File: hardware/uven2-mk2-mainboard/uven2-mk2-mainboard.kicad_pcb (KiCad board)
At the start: 2 copper layers, 121 x 93 mm, 87 parts, among them J1 LED, J10 LED, J11 LED, J12 LED, J13 LED, J14 LED, J15 LED, J16 LED, J2 LED, J3 LED, J4 LED, J5 LED, J6 LED, J7 LED, J8 LED, J9 LED, Q1 QM6006D, Q10 QM6006D, Q11 QM6006D, Q12 QM6006D, Q13 QM6006D, Q14 QM6006D, Q15 QM6006D, Q16 QM6006D, Q2 QM6006D, Q3 QM6006D, Q4 QM6006D, Q5 QM6006D, Q6 QM6006D, Q7 QM6006D, Q8 QM6006D, Q9 QM6006D, U1 DEV-16771, U2 MCP48FEB28T-20E/ST, U3 MCP48FEB28T-20E/ST

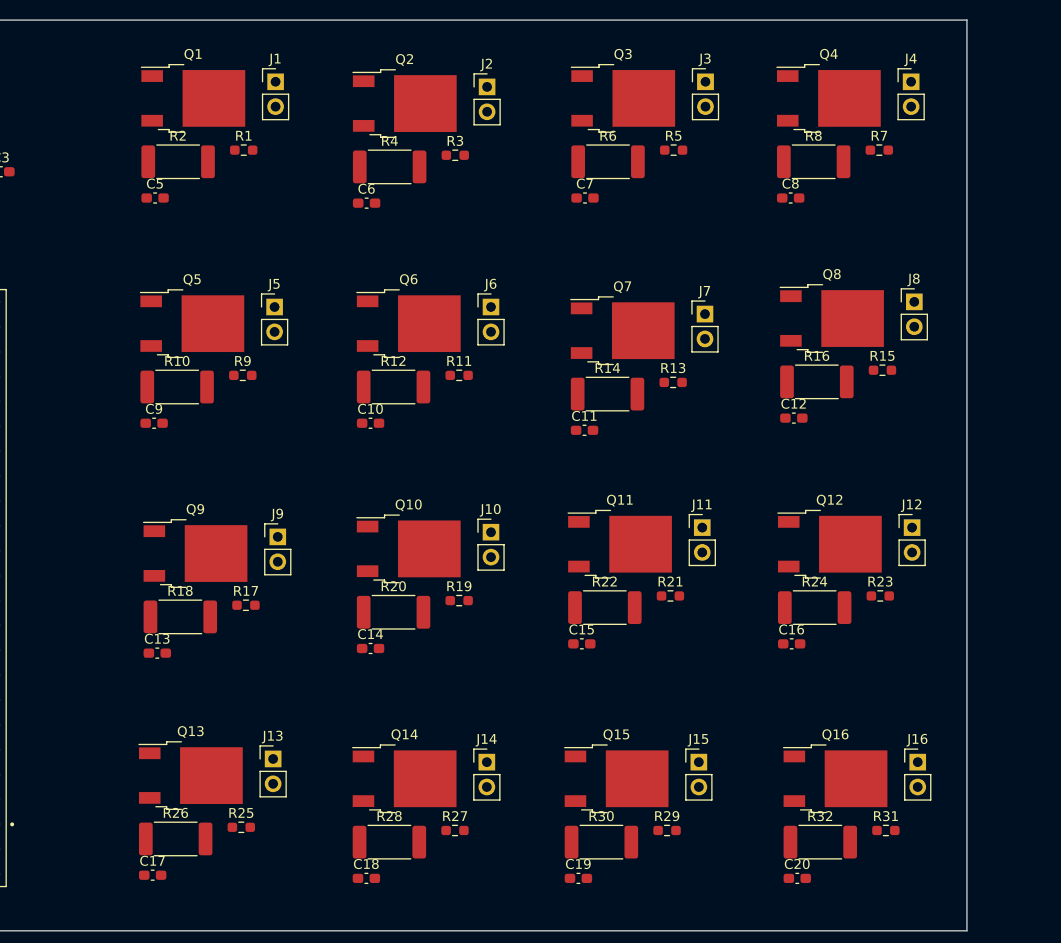
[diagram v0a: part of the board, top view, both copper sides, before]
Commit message: with current limiting switch
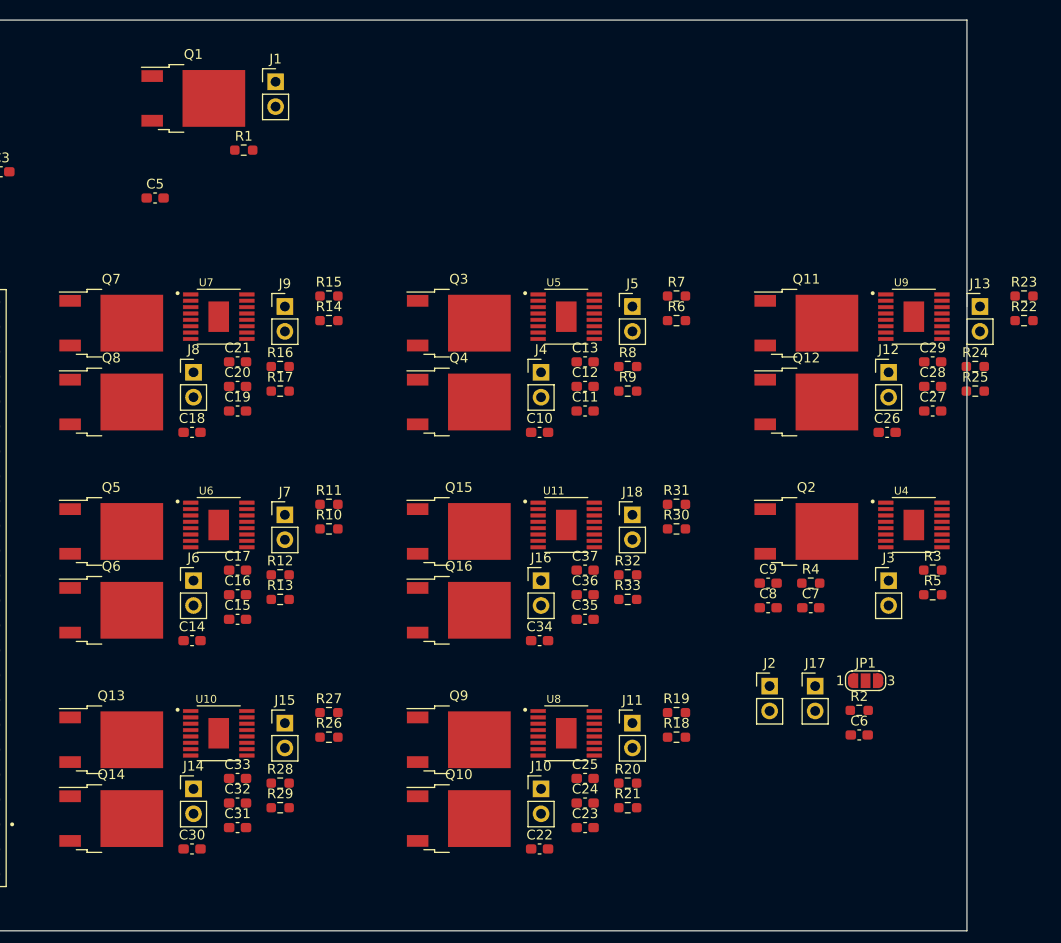
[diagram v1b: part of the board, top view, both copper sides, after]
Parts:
- added C21: 4.7u, Capacitor_SMD:C_0603_1608Metric_Pad1.08x0.95mm_HandSolder, F.Cu at (131.5, 72.9)
- added C22: 100n, Capacitor_SMD:C_0603_1608Metric_Pad1.08x0.95mm_HandSolder, F.Cu at (162.4, 122.6)
- added C23: 100n, Capacitor_SMD:C_0603_1608Metric_Pad1.08x0.95mm_HandSolder, F.Cu at (167.0, 120.5)
- added C24: 220n, Capacitor_SMD:C_0603_1608Metric_Pad1.08x0.95mm_HandSolder, F.Cu at (167.0, 118.0)
- added C25: 4.7u, Capacitor_SMD:C_0603_1608Metric_Pad1.08x0.95mm_HandSolder, F.Cu at (167.0, 115.4)
- added C26: 100n, Capacitor_SMD:C_0603_1608Metric_Pad1.08x0.95mm_HandSolder, F.Cu at (197.8, 80.1)
- added C27: 100n, Capacitor_SMD:C_0603_1608Metric_Pad1.08x0.95mm_HandSolder, F.Cu at (202.5, 77.9)
- added C28: 220n, Capacitor_SMD:C_0603_1608Metric_Pad1.08x0.95mm_HandSolder, F.Cu at (202.5, 75.4)
- added C29: 4.7u, Capacitor_SMD:C_0603_1608Metric_Pad1.08x0.95mm_HandSolder, F.Cu at (202.5, 72.9)
- added C30: 100n, Capacitor_SMD:C_0603_1608Metric_Pad1.08x0.95mm_HandSolder, F.Cu at (126.9, 122.6)
- added C31: 100n, Capacitor_SMD:C_0603_1608Metric_Pad1.08x0.95mm_HandSolder, F.Cu at (131.5, 120.5)
- added C32: 220n, Capacitor_SMD:C_0603_1608Metric_Pad1.08x0.95mm_HandSolder, F.Cu at (131.5, 118.0)
- added C33: 4.7u, Capacitor_SMD:C_0603_1608Metric_Pad1.08x0.95mm_HandSolder, F.Cu at (131.5, 115.4)
- added C34: 100n, Capacitor_SMD:C_0603_1608Metric_Pad1.08x0.95mm_HandSolder, F.Cu at (162.4, 101.4)
- added C35: 100n, Capacitor_SMD:C_0603_1608Metric_Pad1.08x0.95mm_HandSolder, F.Cu at (167.0, 99.2)
- added C36: 220n, Capacitor_SMD:C_0603_1608Metric_Pad1.08x0.95mm_HandSolder, F.Cu at (167.0, 96.7)
- added C37: 4.7u, Capacitor_SMD:C_0603_1608Metric_Pad1.08x0.95mm_HandSolder, F.Cu at (167.0, 94.2)
- added J17: PowerON/OFF, Connector_PinHeader_2.54mm:PinHeader_1x02_P2.54mm_Vertical, F.Cu at (190.5, 106.0)
- added J18: LED, Connector_PinHeader_2.54mm:PinHeader_1x02_P2.54mm_Vertical, F.Cu at (171.8, 88.5)
- added JP1: Vref_select, Jumper:SolderJumper-3_P1.3mm_Open_RoundedPad1.0x1.5mm_NumberLabels, F.Cu at (195.7, 105.5)
- added R33: 10k, Resistor_SMD:R_0603_1608Metric_Pad0.98x0.95mm_HandSolder, F.Cu at (171.4, 97.2)
- added U10: TPS2HB50BQPWPRQ1, custom_lib:SOP65P640X120-17N, F.Cu at (129.6, 110.8)
- added U11: TPS2HB50BQPWPRQ1, custom_lib:SOP65P640X120-17N, F.Cu at (165.1, 89.6)
- added U4: TPS2HB50BQPWPRQ1, custom_lib:SOP65P640X120-17N, F.Cu at (200.6, 89.6)
- added U5: TPS2HB50BQPWPRQ1, custom_lib:SOP65P640X120-17N, F.Cu at (165.1, 68.3)
- added U6: TPS2HB50BQPWPRQ1, custom_lib:SOP65P640X120-17N, F.Cu at (129.6, 89.6)
- added U7: TPS2HB50BQPWPRQ1, custom_lib:SOP65P640X120-17N, F.Cu at (129.6, 68.3)
- added U8: TPS2HB50BQPWPRQ1, custom_lib:SOP65P640X120-17N, F.Cu at (165.1, 110.8)
- added U9: TPS2HB50BQPWPRQ1, custom_lib:SOP65P640X120-17N, F.Cu at (200.6, 68.3)
- C12, C16, C20, C8: value 100n -> 220n
- C13, C17, C9: value 100n -> 4.7u
- C6: value 100n -> 10n
- J2: value LED -> LED_ENABLE
- R10, R14, R18, R2, R22, R26, R30, R6: value 220mOhm -> 1k; footprint Resistor_SMD:R_2512_6332Metric_Pad1.40x3.35mm_HandSolder -> Resistor_SMD:R_0603_1608Metric_Pad0.98x0.95mm_HandSolder
- R12, R16, R20, R24, R28, R32, R4, R8: value 220mOhm -> 10k; footprint Resistor_SMD:R_2512_6332Metric_Pad1.40x3.35mm_HandSolder -> Resistor_SMD:R_0603_1608Metric_Pad0.98x0.95mm_HandSolder
- R13, R17, R21, R25, R29, R5, R9: value 1k -> 10k
- moved R2 89.3 mm to (195.0, 108.5)
- moved R25 87.2 mm to (206.8, 75.9)
- moved J13 85.7 mm to (207.3, 67.2)
- moved C20 76.1 mm to (131.5, 75.4)
- moved Q8 74.1 mm to (118.6, 77.0)
- moved C6 74.0 mm to (195.0, 111.0)
- moved J8 74.0 mm to (127.0, 74.0)
- moved J2 67.6 mm to (185.8, 106.0)
- moved C9 64.8 mm to (185.7, 95.5)
- moved R3 64.6 mm to (202.5, 94.2)
- moved R4 60.5 mm to (190.1, 95.5)
- moved Q2 59.9 mm to (189.6, 90.2)
- moved C19 59.1 mm to (131.5, 77.9)
- moved R15 57.0 mm to (140.8, 66.2)
- moved C16 56.8 mm to (131.5, 96.7)
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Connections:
- C10 pad 2: /GATE_LED5 -> /GATE_LED2
- C11 pad 2: /GATE_LED6 -> /GATE_LED3
- C12 pad 2: /GATE_LED7 -> +24V
- C13 pad 2: /GATE_LED8 -> +24V
- C14 pad 2: /GATE_LED9 -> /GATE_LED4
- C15 pad 2: /GATE_LED10 -> /GATE_LED5
- C16 pad 2: /GATE_LED11 -> +24V
- C17 pad 2: /GATE_LED12 -> +24V
- C18 pad 2: /GATE_LED13 -> /GATE_LED6
- C19 pad 2: /GATE_LED14 -> /GATE_LED7
- C20 pad 2: /GATE_LED15 -> +24V
- C6 pad 1: GND -> /LED_SENS
- C6 pad 2: /GATE_LED1 -> GND
- C7 pad 2: /GATE_LED2 -> /GATE_LED1
- C8 pad 2: /GATE_LED3 -> +24V
- C9 pad 2: /GATE_LED4 -> +24V
- J1 pad 1: +24V -> unconnected-(J1-Pad1)
- J10 pad 1: +24V -> unconnected-(J10-Pad1)
- J11 pad 1: +24V -> unconnected-(J11-Pad1)
- J12 pad 1: +24V -> unconnected-(J12-Pad1)
- J13 pad 1: +24V -> unconnected-(J13-Pad1)
- J14 pad 1: +24V -> unconnected-(J14-Pad1)
- J15 pad 1: +24V -> unconnected-(J15-Pad1)
- J16 pad 1: +24V -> unconnected-(J16-Pad1)
- J2 pad 1: +24V -> GND
- J2 pad 2: Net-(J2-Pad2) -> /LED_ENABLE
- J3 pad 1: +24V -> unconnected-(J3-Pad1)
- J4 pad 1: +24V -> unconnected-(J4-Pad1)
- J5 pad 1: +24V -> unconnected-(J5-Pad1)
- J6 pad 1: +24V -> unconnected-(J6-Pad1)
- J7 pad 1: +24V -> unconnected-(J7-Pad1)
- J8 pad 1: +24V -> unconnected-(J8-Pad1)
- J9 pad 1: +24V -> unconnected-(J9-Pad1)
- Q1 pad 3: /SHUNT_LED0 -> GND
- Q10 pad 2: Net-(J10-Pad2) -> Net-(J11-Pad2)
- Q10 pad 3: /SHUNT_LED9 -> GND
- Q11 pad 2: Net-(J11-Pad2) -> Net-(J12-Pad2)
- Q11 pad 3: /SHUNT_LED10 -> GND
- Q12 pad 2: Net-(J12-Pad2) -> Net-(J13-Pad2)
- Q12 pad 3: /SHUNT_LED11 -> GND
- Q13 pad 2: Net-(J13-Pad2) -> Net-(J14-Pad2)
- Q13 pad 3: /SHUNT_LED12 -> GND
- Q14 pad 2: Net-(J14-Pad2) -> Net-(J15-Pad2)
- Q14 pad 3: /SHUNT_LED13 -> GND
- Q15 pad 2: Net-(J15-Pad2) -> Net-(J16-Pad2)
- Q15 pad 3: /SHUNT_LED14 -> GND
- Q16 pad 2: Net-(J16-Pad2) -> Net-(J18-Pad2)
- Q16 pad 3: /SHUNT_LED15 -> GND
- Q2 pad 2: Net-(J2-Pad2) -> Net-(J3-Pad2)
- Q2 pad 3: /SHUNT_LED1 -> GND
- Q3 pad 2: Net-(J3-Pad2) -> Net-(J4-Pad2)
- Q3 pad 3: /SHUNT_LED2 -> GND
- Q4 pad 2: Net-(J4-Pad2) -> Net-(J5-Pad2)
- Q4 pad 3: /SHUNT_LED3 -> GND
- Q5 pad 2: Net-(J5-Pad2) -> Net-(J6-Pad2)
- Q5 pad 3: /SHUNT_LED4 -> GND
- Q6 pad 2: Net-(J6-Pad2) -> Net-(J7-Pad2)
- Q6 pad 3: /SHUNT_LED5 -> GND
- Q7 pad 2: Net-(J7-Pad2) -> Net-(J8-Pad2)
- Q7 pad 3: /SHUNT_LED6 -> GND
- Q8 pad 2: Net-(J8-Pad2) -> Net-(J9-Pad2)
- Q8 pad 3: /SHUNT_LED7 -> GND
- Q9 pad 2: Net-(J9-Pad2) -> Net-(J10-Pad2)
- Q9 pad 3: /SHUNT_LED8 -> GND
- R10 pad 1: /SHUNT_LED4 -> GND
- R10 pad 2: GND -> /GATE_LED4
- R12 pad 1: /SHUNT_LED5 -> +24V
- R12 pad 2: GND -> Net-(R12-Pad2)
- R13 pad 1: GND -> +24V
- R13 pad 2: /GATE_LED6 -> Net-(R13-Pad2)
- R14 pad 1: /SHUNT_LED6 -> GND
- R14 pad 2: GND -> /GATE_LED6
- R16 pad 1: /SHUNT_LED7 -> +24V
- R16 pad 2: GND -> Net-(R16-Pad2)
- R17 pad 1: GND -> +24V
- R17 pad 2: /GATE_LED8 -> Net-(R17-Pad2)
- R18 pad 1: /SHUNT_LED8 -> GND
- R18 pad 2: GND -> /GATE_LED8
- R2 pad 1: /SHUNT_LED0 -> /LED_SENS
- R20 pad 1: /SHUNT_LED9 -> +24V
- R20 pad 2: GND -> Net-(R20-Pad2)
- R21 pad 1: GND -> +24V
- R21 pad 2: /GATE_LED10 -> Net-(R21-Pad2)
- R22 pad 1: /SHUNT_LED10 -> GND
- R22 pad 2: GND -> /GATE_LED10
- R24 pad 1: /SHUNT_LED11 -> +24V
- R24 pad 2: GND -> Net-(R24-Pad2)
- R25 pad 1: GND -> +24V
- R25 pad 2: /GATE_LED12 -> Net-(R25-Pad2)
- R26 pad 1: /SHUNT_LED12 -> GND
- R26 pad 2: GND -> /GATE_LED12
- R28 pad 1: /SHUNT_LED13 -> +24V
- R28 pad 2: GND -> Net-(R28-Pad2)
- R29 pad 1: GND -> +24V
- R29 pad 2: /GATE_LED14 -> Net-(R29-Pad2)
- R30 pad 1: /SHUNT_LED14 -> GND
- R30 pad 2: GND -> /GATE_LED14
- R32 pad 1: /SHUNT_LED15 -> +24V
- R32 pad 2: GND -> Net-(R32-Pad2)
- R4 pad 1: /SHUNT_LED1 -> +24V
- R4 pad 2: GND -> Net-(R4-Pad2)
- R5 pad 1: GND -> +24V
- R5 pad 2: /GATE_LED2 -> Net-(R5-Pad2)
- R6 pad 1: /SHUNT_LED2 -> GND
- R6 pad 2: GND -> /GATE_LED2
- R8 pad 1: /SHUNT_LED3 -> +24V
- R8 pad 2: GND -> Net-(R8-Pad2)
- R9 pad 1: GND -> +24V
- R9 pad 2: /GATE_LED4 -> Net-(R9-Pad2)
- U1 pad 14: /SHUNT_LED0 -> /LED_SENS
- U1 pad 15: /SHUNT_LED1 -> /LED_DIAG_ENABLE_A
- U1 pad 16: /SHUNT_LED2 -> /LED_DIAG_ENABLE_B
- U1 pad 17: /SHUNT_LED3 -> /LED_DIAG_ENABLE_C
- U1 pad 18: /SHUNT_LED4 -> /LED_DIAG_ENABLE_D
- U1 pad 19: /SHUNT_LED5 -> /LED_DIAG_ENABLE_E
- U1 pad 20: /SHUNT_LED6 -> /LED_DIAG_ENABLE_F
- U1 pad 21: /SHUNT_LED7 -> /LED_DIAG_ENABLE_G
- U1 pad 22: /SHUNT_LED8 -> /LED_DIAG_ENABLE_H
- U1 pad 23: /SHUNT_LED9 -> /LED_ENABLE
- U1 pad 24: /SHUNT_LED10 -> /LED_LATCH
- U1 pad 25: /SHUNT_LED11 -> /LED0_SEL
- U1 pad 26: /SHUNT_LED12 -> /LED1_SEL
- U1 pad 27: /SHUNT_LED13 -> /LATCH0
- U1 pad 38: /SHUNT_LED14 -> /LATCH1
- U1 pad 39: /SHUNT_LED15 -> unconnected-(U1-Pad39)
- U1 pad 5V: unconnected-(U1-Pad5V) -> +5V
- U1 pad GND1: Net-(U1-PadGND1) -> GND
- U1 pad GND2: Net-(U1-PadGND1) -> GND
- U1 pad GND3: Net-(U1-PadGND1) -> GND
- U1 pad GND4: Net-(U1-PadGND1) -> GND
- U1 pad GND5: Net-(U1-PadGND1) -> GND
- U1 pad ON/OFF: unconnected-(U1-PadON/OFF) -> /PowerON/OFF
- U1 pad USB_GND1: Net-(U1-PadUSB_GND1) -> GND
- U1 pad USB_GND2: Net-(U1-PadUSB_GND1) -> GND
- U2 pad 16: +3.3V -> Net-(U2-Pad16)
- U2 pad 4: +3.3V -> Net-(U2-Pad16)

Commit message: with wago connector
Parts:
- removed J10, J11, J12, J13, J14, J15, J16, J18, J3, J4, J5, J6, J7, J8, J9: LED, Connector_PinHeader_2.54mm:PinHeader_1x02_P2.54mm_Vertical
- J1: value LED -> 713-1436_037-000; footprint Connector_PinHeader_2.54mm:PinHeader_1x02_P2.54mm_Vertical -> custom_lib:CONN_713-1436&slash_037-000_WAG
- moved J1 63.7 mm to (199.0, 48.0), turned to 180 degrees
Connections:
- J1 pad 1: unconnected-(J1-Pad1) -> /LED0-
- J1 pad 2: Net-(J1-Pad2) -> /LED0+
- Q1 pad 2: Net-(J1-Pad2) -> /LED0-
- Q10 pad 2: Net-(J11-Pad2) -> /LED9-
- Q11 pad 2: Net-(J12-Pad2) -> /LED10-
- Q12 pad 2: Net-(J13-Pad2) -> /LED11-
- Q13 pad 2: Net-(J14-Pad2) -> /LED12-
- Q14 pad 2: Net-(J15-Pad2) -> /LED13-
- Q15 pad 2: Net-(J16-Pad2) -> /LED14-
- Q16 pad 2: Net-(J18-Pad2) -> /LED15-
- Q2 pad 2: Net-(J3-Pad2) -> /LED1-
- Q3 pad 2: Net-(J4-Pad2) -> /LED2-
- Q4 pad 2: Net-(J5-Pad2) -> /LED3-
- Q5 pad 2: Net-(J6-Pad2) -> /LED4-
- Q6 pad 2: Net-(J7-Pad2) -> /LED5-
- Q7 pad 2: Net-(J8-Pad2) -> /LED6-
- Q8 pad 2: Net-(J9-Pad2) -> /LED7-
- Q9 pad 2: Net-(J10-Pad2) -> /LED8-
- U1 pad 15: /LED_DIAG_ENABLE_A -> /TEMP_LED0
- U1 pad 16: /LED_DIAG_ENABLE_B -> /TEMP_LED1
- U1 pad 17: /LED_DIAG_ENABLE_C -> /TEMP_LED2
- U1 pad 18: /LED_DIAG_ENABLE_D -> /TEMP_LED3
- U1 pad 19: /LED_DIAG_ENABLE_E -> /TEMP_LED4
- U1 pad 2: unconnected-(U1-Pad2) -> /LED_ENABLE
- U1 pad 20: /LED_DIAG_ENABLE_F -> /TEMP_LED5
- U1 pad 21: /LED_DIAG_ENABLE_G -> /TEMP_LED6
- U1 pad 22: /LED_DIAG_ENABLE_H -> /TEMP_LED7
- U1 pad 23: /LED_ENABLE -> /TEMP_LED8
- U1 pad 24: /LED_LATCH -> /TEMP_LED9
- U1 pad 25: /LED0_SEL -> /TEMP_LED10
- U1 pad 26: /LED1_SEL -> /TEMP_LED11
- U1 pad 27: /LATCH0 -> /TEMP_LED12
- U1 pad 28: unconnected-(U1-Pad28) -> /LED_DIAG_ENABLE_C
- U1 pad 29: unconnected-(U1-Pad29) -> /LED_DIAG_ENABLE_D
- U1 pad 3: unconnected-(U1-Pad3) -> /LED_LATCH
- U1 pad 30: unconnected-(U1-Pad30) -> /LED_DIAG_ENABLE_E
- U1 pad 31: unconnected-(U1-Pad31) -> /LED_DIAG_ENABLE_F
- U1 pad 33: unconnected-(U1-Pad33) -> /LED_DIAG_ENABLE_G
- U1 pad 34: unconnected-(U1-Pad34) -> /LED_DIAG_ENABLE_H
- U1 pad 38: /LATCH1 -> /TEMP_LED13
- U1 pad 39: unconnected-(U1-Pad39) -> /TEMP_LED14
- U1 pad 4: unconnected-(U1-Pad4) -> /LED0_SEL
- U1 pad 40: unconnected-(U1-Pad40) -> /TEMP_LED15
- U1 pad 5: unconnected-(U1-Pad5) -> /LED1_SEL
- U1 pad 6: unconnected-(U1-Pad6) -> /LATCH0
- U1 pad 7: unconnected-(U1-Pad7) -> /LATCH1
- U1 pad 8: unconnected-(U1-Pad8) -> /LED_DIAG_ENABLE_A
- U1 pad 9: unconnected-(U1-Pad9) -> /LED_DIAG_ENABLE_B
- U10 pad 10: /LED Driver6/LED1 -> /LED13+
- U10 pad 11: /LED Driver6/LED1 -> /LED13+
- U10 pad 6: /LED Driver6/LED0 -> /LED12+
- U10 pad 7: /LED Driver6/LED0 -> /LED12+
- U10 pad 8: /LED Driver6/LED0 -> /LED12+
- U10 pad 9: /LED Driver6/LED1 -> /LED13+
- U11 pad 10: /LED Driver7/LED1 -> /LED15+
- U11 pad 11: /LED Driver7/LED1 -> /LED15+
- U11 pad 6: /LED Driver7/LED0 -> /LED14+
- U11 pad 7: /LED Driver7/LED0 -> /LED14+
- U11 pad 8: /LED Driver7/LED0 -> /LED14+
- U11 pad 9: /LED Driver7/LED1 -> /LED15+
- U4 pad 10: /LED Driver/LED1 -> /LED1+
- U4 pad 11: /LED Driver/LED1 -> /LED1+
- U4 pad 6: /LED Driver/LED0 -> /LED0+
- U4 pad 7: /LED Driver/LED0 -> /LED0+
- U4 pad 8: /LED Driver/LED0 -> /LED0+
- U4 pad 9: /LED Driver/LED1 -> /LED1+
- U5 pad 10: /LED Driver1/LED1 -> /LED3+
- U5 pad 11: /LED Driver1/LED1 -> /LED3+
- U5 pad 6: /LED Driver1/LED0 -> /LED2+
- U5 pad 7: /LED Driver1/LED0 -> /LED2+
- U5 pad 8: /LED Driver1/LED0 -> /LED2+
- U5 pad 9: /LED Driver1/LED1 -> /LED3+
- U6 pad 10: /LED Driver2/LED1 -> /LED5+
- U6 pad 11: /LED Driver2/LED1 -> /LED5+
- U6 pad 6: /LED Driver2/LED0 -> /LED4+
- U6 pad 7: /LED Driver2/LED0 -> /LED4+
- U6 pad 8: /LED Driver2/LED0 -> /LED4+
- U6 pad 9: /LED Driver2/LED1 -> /LED5+
- U7 pad 10: /LED Driver3/LED1 -> /LED7+
- U7 pad 11: /LED Driver3/LED1 -> /LED7+
- U7 pad 6: /LED Driver3/LED0 -> /LED6+
- U7 pad 7: /LED Driver3/LED0 -> /LED6+
- U7 pad 8: /LED Driver3/LED0 -> /LED6+
- U7 pad 9: /LED Driver3/LED1 -> /LED7+
- U8 pad 10: /LED Driver4/LED1 -> /LED9+
- U8 pad 11: /LED Driver4/LED1 -> /LED9+
- U8 pad 6: /LED Driver4/LED0 -> /LED8+
- U8 pad 7: /LED Driver4/LED0 -> /LED8+
- U8 pad 8: /LED Driver4/LED0 -> /LED8+
- U8 pad 9: /LED Driver4/LED1 -> /LED9+
- U9 pad 10: /LED Driver5/LED1 -> /LED11+
- U9 pad 11: /LED Driver5/LED1 -> /LED11+
- U9 pad 6: /LED Driver5/LED0 -> /LED10+
- U9 pad 7: /LED Driver5/LED0 -> /LED10+
- U9 pad 8: /LED Driver5/LED0 -> /LED10+
- U9 pad 9: /LED Driver5/LED1 -> /LED11+

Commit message: with different mosfet
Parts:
- removed Q1, Q10, Q11, Q12, Q13, Q14, Q15, Q16, Q2, Q3, Q4, Q5, Q6, Q7, Q8, Q9: QM6006D, Package_TO_SOT_SMD:TO-252-2
- added U12: SIDR392DP-T1-GE3, custom_lib:PowerPAK SO-8DC, F.Cu at (143.0, 74.0)
- added U13: SIDR392DP-T1-GE3, custom_lib:PowerPAK SO-8DC, F.Cu at (142.0, 79.0)
- added U14: SIDR392DP-T1-GE3, custom_lib:PowerPAK SO-8DC, F.Cu at (179.0, 73.0)
- added U15: SIDR392DP-T1-GE3, custom_lib:PowerPAK SO-8DC, F.Cu at (178.7, 78.4)
- added U16: SIDR392DP-T1-GE3, custom_lib:PowerPAK SO-8DC, F.Cu at (144.3, 95.0)
- added U17: SIDR392DP-T1-GE3, custom_lib:PowerPAK SO-8DC, F.Cu at (144.0, 101.0)
- added U18: SIDR392DP-T1-GE3, custom_lib:PowerPAK SO-8DC, F.Cu at (149.3, 64.0)
- added U19: SIDR392DP-T1-GE3, custom_lib:PowerPAK SO-8DC, F.Cu at (190.0, 71.0)
- added U20: SIDR392DP-T1-GE3, custom_lib:PowerPAK SO-8DC, F.Cu at (178.4, 123.0)
- added U21: SIDR392DP-T1-GE3, custom_lib:PowerPAK SO-8DC, F.Cu at (186.0, 123.0)
- added U22: SIDR392DP-T1-GE3, custom_lib:PowerPAK SO-8DC, F.Cu at (159.1, 58.6)
- added U23: SIDR392DP-T1-GE3, custom_lib:PowerPAK SO-8DC, F.Cu at (166.7, 58.6)
- added U24: SIDR392DP-T1-GE3, custom_lib:PowerPAK SO-8DC, F.Cu at (142.7, 118.0)
- added U25: SIDR392DP-T1-GE3, custom_lib:PowerPAK SO-8DC, F.Cu at (150.3, 118.0)
- added U26: SIDR392DP-T1-GE3, custom_lib:PowerPAK SO-8DC, F.Cu at (169.4, 103.8)
- added U27: SIDR392DP-T1-GE3, custom_lib:PowerPAK SO-8DC, F.Cu at (177.0, 103.0)

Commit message: schematics done
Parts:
- added C38: 100n, Capacitor_SMD:C_0603_1608Metric_Pad1.08x0.95mm_HandSolder, F.Cu at (72.0, 73.0)
- added J10: GND, custom_lib:7466205R, F.Cu at (229.0, 130.0)
- added J11: 24V, custom_lib:7466205R, F.Cu at (229.0, 118.0)
- added J12: GND, custom_lib:7466205R, F.Cu at (229.0, 68.0)
- added J13: 24V, custom_lib:7466205R, F.Cu at (229.0, 106.0)
- added J14: GND, custom_lib:7466205R, F.Cu at (229.0, 94.0)
- added J15: Chamber_Control, Connector_Dsub:DSUB-37_Female_Horizontal_P2.77x2.84mm_EdgePinOffset7.70mm_Housed_MountingHolesOffset9.12mm, F.Cu at (102.1, 54.4)
- added J3: 5V, custom_lib:KEYSTONE_7767, F.Cu at (94.0, 131.0)
- added J4: GND, custom_lib:KEYSTONE_7767, F.Cu at (73.0, 131.0)
- added J5: J1B1211CCD, custom_lib:J1B1211CCD, F.Cu at (79.0, 47.0)
- added J6: 24V, custom_lib:KEYSTONE_7767, F.Cu at (83.5, 130.5)
- added J7: GND, custom_lib:KEYSTONE_7767, F.Cu at (105.0, 131.0)
- added J8: USB_HOST, Connector_PinHeader_2.54mm:PinHeader_1x05_P2.54mm_Vertical, F.Cu at (72.0, 118.1)
- added J9: 24V, custom_lib:7466205R, F.Cu at (229.0, 80.0)
- added JP2: Vref_select, Jumper:SolderJumper-3_P1.3mm_Open_RoundedPad1.0x1.5mm_NumberLabels, F.Cu at (78.7, 65.5)
- added Q1: 2N7002, Package_TO_SOT_SMD:SOT-23, F.Cu at (84.0, 66.0)
- added Q2: 2N7002, Package_TO_SOT_SMD:SOT-23, F.Cu at (78.3, 69.5)
- added R34: 10k, Resistor_SMD:R_0603_1608Metric_Pad0.98x0.95mm_HandSolder, F.Cu at (105.0, 68.5)
- added R35: 10k, Resistor_SMD:R_0603_1608Metric_Pad0.98x0.95mm_HandSolder, F.Cu at (105.0, 71.0)
- added R36: 10k, Resistor_SMD:R_0603_1608Metric_Pad0.98x0.95mm_HandSolder, F.Cu at (111.0, 76.5)
- added R37: 10k, Resistor_SMD:R_0603_1608Metric_Pad0.98x0.95mm_HandSolder, F.Cu at (111.0, 79.0)
- added R38: 10k, Resistor_SMD:R_0603_1608Metric_Pad0.98x0.95mm_HandSolder, F.Cu at (116.2, 60.3)
- added R39: 10k, Resistor_SMD:R_0603_1608Metric_Pad0.98x0.95mm_HandSolder, F.Cu at (116.2, 62.8)
- added R40: 10k, Resistor_SMD:R_0603_1608Metric_Pad0.98x0.95mm_HandSolder, F.Cu at (111.0, 68.5)
- added R41: 10k, Resistor_SMD:R_0603_1608Metric_Pad0.98x0.95mm_HandSolder, F.Cu at (111.0, 71.0)
- added R42: 10k, Resistor_SMD:R_0603_1608Metric_Pad0.98x0.95mm_HandSolder, F.Cu at (105.0, 76.5)
- added R43: 10k, Resistor_SMD:R_0603_1608Metric_Pad0.98x0.95mm_HandSolder, F.Cu at (105.0, 79.0)
- added R44: 10k, Resistor_SMD:R_0603_1608Metric_Pad0.98x0.95mm_HandSolder, F.Cu at (116.0, 76.5)
- added R45: 10k, Resistor_SMD:R_0603_1608Metric_Pad0.98x0.95mm_HandSolder, F.Cu at (116.0, 79.0)
- added R46: 10k, Resistor_SMD:R_0603_1608Metric_Pad0.98x0.95mm_HandSolder, F.Cu at (116.0, 68.5)
- added R47: 10k, Resistor_SMD:R_0603_1608Metric_Pad0.98x0.95mm_HandSolder, F.Cu at (116.0, 71.0)
- added R48: 10k, Resistor_SMD:R_0603_1608Metric_Pad0.98x0.95mm_HandSolder, F.Cu at (105.2, 60.4)
- added R49: 10k, Resistor_SMD:R_0603_1608Metric_Pad0.98x0.95mm_HandSolder, F.Cu at (105.2, 62.9)
- added R50: 1k, Resistor_SMD:R_0603_1608Metric_Pad0.98x0.95mm_HandSolder, F.Cu at (111.0, 62.8)
- added R51: 10k, Resistor_SMD:R_0603_1608Metric_Pad0.98x0.95mm_HandSolder, F.Cu at (121.0, 61.0)
- added R52: 10k, Resistor_SMD:R_0603_1608Metric_Pad0.98x0.95mm_HandSolder, F.Cu at (111.0, 60.3)
- added TP1: 5V, custom_lib:TP420X150, F.Cu at (214.5, 117.3)
- added TP10: LED_DIAG_ENABLE_E, custom_lib:TP420X150, F.Cu at (88.0, 113.9)
- added TP11: LED_DIAG_ENABLE_F, custom_lib:TP420X150, F.Cu at (99.5, 110.7)
- added TP12: LED_LATCH, custom_lib:TP420X150, F.Cu at (90.1, 107.6)
- added TP13: LED0_SEL, custom_lib:TP420X150, F.Cu at (84.2, 86.9)
- added TP14: LED_DIAG_ENABLE_G, custom_lib:TP420X150, F.Cu at (99.5, 113.9)
- added TP15: SCK, custom_lib:TP420X150, F.Cu at (105.2, 120.2)
- added TP16: LED_SENS, custom_lib:TP420X150, F.Cu at (221.0, 60.0)
- added TP17: TEMP_LED0, custom_lib:TP420X150, F.Cu at (84.2, 77.4)
- added TP18: TEMP_LED1, custom_lib:TP420X150, F.Cu at (95.0, 66.0)
- added TP19: TEMP_LED2, custom_lib:TP420X150, F.Cu at (210.8, 123.6)
- added TP2: GND, custom_lib:TP420X150, F.Cu at (208.8, 117.3)
- added TP20: TEMP_LED3, custom_lib:TP420X150, F.Cu at (74.8, 93.1)
- added TP21: TEMP_LED4, custom_lib:TP420X150, F.Cu at (80.5, 93.1)
- added TP22: TEMP_LED5, custom_lib:TP420X150, F.Cu at (84.2, 80.6)
- added TP23: TEMP_LED6, custom_lib:TP420X150, F.Cu at (105.2, 110.7)
- added TP24: TEMP_LED7, custom_lib:TP420X150, F.Cu at (98.0, 76.0)
- added TP25: 24V_FANS, custom_lib:TP420X150, F.Cu at (82.2, 113.9)
- added TP26: GND, custom_lib:TP420X150, F.Cu at (78.5, 77.4)
- added TP27: 24V_LEDS, custom_lib:TP420X150, F.Cu at (205.1, 123.6)
- added TP28: GND, custom_lib:TP420X150, F.Cu at (86.3, 93.2)
- added TP29: LED_ENABLE, custom_lib:TP420X150, F.Cu at (203.0, 117.3)
- added TP3: LED1_SEL, custom_lib:TP420X150, F.Cu at (208.8, 120.5)
- added TP30: LATCH0, custom_lib:TP420X150, F.Cu at (95.0, 62.9)
- added TP31: LED_DIAG_ENABLE_B, custom_lib:TP420X150, F.Cu at (84.2, 83.7)
- added TP32: LED_DIAG_ENABLE_D, custom_lib:TP420X150, F.Cu at (105.2, 113.9)
- added TP33: CS0, custom_lib:TP420X150, F.Cu at (74.8, 96.3)
- added TP34: CS1, custom_lib:TP420X150, F.Cu at (86.3, 99.5)
- added TP35: MISO, custom_lib:TP420X150, F.Cu at (201.0, 57.0)
- added TP36: MOSI, custom_lib:TP420X150, F.Cu at (214.5, 114.2)
- added TP37: LED_DIAG_ENABLE_C, custom_lib:TP420X150, F.Cu at (105.2, 117.0)
- added TP38: TEMP_LED15, custom_lib:TP420X150, F.Cu at (74.8, 99.4)
- added TP39: TEMP_LED14, custom_lib:TP420X150, F.Cu at (214.5, 111.0)
- added TP4: PowerON/OFF, custom_lib:TP420X150, F.Cu at (84.3, 107.6)
- added TP40: TEMP_LED13, custom_lib:TP420X150, F.Cu at (78.5, 86.8)
- added TP41: TEMP_LED12, custom_lib:TP420X150, F.Cu at (99.5, 120.2)
- added TP42: TEMP_LED11, custom_lib:TP420X150, F.Cu at (80.5, 96.3)
- added TP43: TEMP_LED10, custom_lib:TP420X150, F.Cu at (72.7, 83.7)
- added TP44: TEMP_LED9, custom_lib:TP420X150, F.Cu at (80.5, 99.4)
- added TP45: TEMP_LED8, custom_lib:TP420X150, F.Cu at (111.0, 111.8)
- added TP46: GATE_LED0, custom_lib:TP420X150, F.Cu at (201.0, 53.9)
- added TP47: GATE_LED1, custom_lib:TP420X150, F.Cu at (205.1, 133.1)
- added TP48: GATE_LED2, custom_lib:TP420X150, F.Cu at (88.0, 117.0)
- added TP49: GATE_LED3, custom_lib:TP420X150, F.Cu at (98.0, 72.8)
- added TP5: LATCH1, custom_lib:TP420X150, F.Cu at (86.3, 96.3)
- added TP50: GATE_LED4, custom_lib:TP420X150, F.Cu at (216.6, 120.5)
- added TP51: GATE_LED5, custom_lib:TP420X150, F.Cu at (93.8, 113.9)
- added TP52: GATE_LED6, custom_lib:TP420X150, F.Cu at (72.7, 80.5)
- added TP53: GATE_LED7, custom_lib:TP420X150, F.Cu at (205.1, 126.8)
- added TP54: GATE_LED8, custom_lib:TP420X150, F.Cu at (88.0, 110.7)
- added TP55: GATE_LED9, custom_lib:TP420X150, F.Cu at (78.5, 90.0)
- added TP56: GATE_LED10, custom_lib:TP420X150, F.Cu at (216.6, 123.6)
- added TP57: GATE_LED11, custom_lib:TP420X150, F.Cu at (69.0, 96.1)
- added TP58: GATE_LED12, custom_lib:TP420X150, F.Cu at (117.0, 118.0)
- added TP59: GATE_LED13, custom_lib:TP420X150, F.Cu at (93.8, 110.7)
- added TP6: LED_DIAG_ENABLE_A, custom_lib:TP420X150, F.Cu at (208.8, 114.2)
- added TP60: GATE_LED14, custom_lib:TP420X150, F.Cu at (84.3, 104.4)
- added TP61: GATE_LED15, custom_lib:TP420X150, F.Cu at (203.0, 120.5)
- added TP62: LED15+, custom_lib:TP420X150, F.Cu at (182.2, 58.5)
- added TP63: LED15-, custom_lib:TP420X150, F.Cu at (72.7, 90.0)
- added TP64: LED14+, custom_lib:TP420X150, F.Cu at (208.8, 111.0)
- added TP65: LED14-, custom_lib:TP420X150, F.Cu at (72.7, 77.4)
- added TP66: LED13+, custom_lib:TP420X150, F.Cu at (82.2, 120.2)
- added TP67: LED13-, custom_lib:TP420X150, F.Cu at (78.5, 80.5)
- added TP68: LED12+, custom_lib:TP420X150, F.Cu at (93.8, 117.0)
- added TP69: LED12-, custom_lib:TP420X150, F.Cu at (82.2, 110.7)
- added TP7: LED_FAN, custom_lib:TP420X150, F.Cu at (187.9, 58.5)
- added TP70: LED11+, custom_lib:TP420X150, F.Cu at (90.1, 104.4)
- added TP71: LED11-, custom_lib:TP420X150, F.Cu at (95.8, 104.4)
- added TP72: LED10+, custom_lib:TP420X150, F.Cu at (93.8, 120.2)
- added TP73: LED10-, custom_lib:TP420X150, F.Cu at (217.3, 65.1)
- added TP74: LED9+, custom_lib:TP420X150, F.Cu at (220.2, 111.0)
- added TP75: LED9-, custom_lib:TP420X150, F.Cu at (210.8, 126.8)
- added TP76: LED8+, custom_lib:TP420X150, F.Cu at (111.0, 115.0)
- added TP77: LED8-, custom_lib:TP420X150, F.Cu at (86.3, 90.0)
- added TP78: LED7+, custom_lib:TP420X150, F.Cu at (193.7, 58.5)
- added TP79: LED7-, custom_lib:TP420X150, F.Cu at (78.5, 83.7)
- added TP8: CHAMBER_FAN, custom_lib:TP420X150, F.Cu at (69.0, 99.3)
- added TP80: LED6+, custom_lib:TP420X150, F.Cu at (205.1, 129.9)
- added TP81: LED6-, custom_lib:TP420X150, F.Cu at (221.0, 53.7)
- added TP82: LED5+, custom_lib:TP420X150, F.Cu at (118.0, 109.0)
- added TP83: LED5-, custom_lib:TP420X150, F.Cu at (101.6, 107.6)
- added TP84: LED4+, custom_lib:TP420X150, F.Cu at (117.0, 114.8)
- added TP85: LED4-, custom_lib:TP420X150, F.Cu at (101.6, 104.4)
- added TP86: LED3+, custom_lib:TP420X150, F.Cu at (203.0, 111.0)
- added TP87: LED3-, custom_lib:TP420X150, F.Cu at (99.5, 117.0)
- added TP88: LED2+, custom_lib:TP420X150, F.Cu at (221.0, 56.9)
- added TP89: LED2-, custom_lib:TP420X150, F.Cu at (118.0, 105.8)
- added TP9: LED_DIAG_ENABLE_H, custom_lib:TP420X150, F.Cu at (82.2, 117.0)
- added TP90: LED1+, custom_lib:TP420X150, F.Cu at (88.0, 120.2)
- added TP91: LED1-, custom_lib:TP420X150, F.Cu at (203.0, 114.2)
- added TP92: LED0+, custom_lib:TP420X150, F.Cu at (72.7, 86.8)
- added TP93: LED0-, custom_lib:TP420X150, F.Cu at (95.8, 107.6)
- J1: value 713-1436_037-000 -> LEDs
- J2: value LED_ENABLE -> 1-282834-0; footprint Connector_PinHeader_2.54mm:PinHeader_1x02_P2.54mm_Vertical -> custom_lib:TE_1-282834-0
- moved J2 145.7 mm to (56.0, 40.0)
- moved U1 43.0 mm to (56.0, 95.0)
- moved C1 41.1 mm to (108.0, 89.0)
- moved C4 41.1 mm to (106.0, 97.0)
- moved U2 41.1 mm to (99.0, 87.0)
- moved U3 41.1 mm to (99.4, 97.3)
- moved C2 41.1 mm to (106.0, 94.5)
- moved C3 41.1 mm to (110.3, 94.5)
- moved C5 36.7 mm to (145.9, 84.9)
- moved R1 36.7 mm to (155.0, 80.0)
- moved J1 27.3 mm to (226.3, 45.8)
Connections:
- J17 pad 2: GND -> unconnected-(J17-Pad2)
- U1 pad 10: /CS0 -> unconnected-(U1-Pad10)
- U1 pad 2: /LED_ENABLE -> Net-(U1-Pad2)
- U1 pad 28: /LED_DIAG_ENABLE_C -> /LED_FAN
- U1 pad 29: /LED_DIAG_ENABLE_D -> /CHAMBER_FAN
- U1 pad 32: unconnected-(U1-Pad32) -> /LED_DIAG_ENABLE_D
- U1 pad 35: unconnected-(U1-Pad35) -> /GPIO_0
- U1 pad 37: unconnected-(U1-Pad37) -> /CS0
- U1 pad 41: unconnected-(U1-Pad41) -> /LED_DIAG_ENABLE_C
- U1 pad 5V: +5V -> unconnected-(U1-Pad5V)
- U1 pad D+: unconnected-(U1-PadD+) -> /USB_HOST_D+
- U1 pad D-: unconnected-(U1-PadD-) -> /USB_HOST_D-
- U1 pad LED: unconnected-(U1-PadLED) -> /ETH_LED
- U1 pad R+: unconnected-(U1-PadR+) -> /ETH_RX+
- U1 pad R-: unconnected-(U1-PadR-) -> /ETH_RX-
- U1 pad T+: unconnected-(U1-PadT+) -> /ETH_TX+
- U1 pad T-: unconnected-(U1-PadT-) -> /ETH_TX-
- U1 pad VIN: unconnected-(U1-PadVIN) -> +5V
- U3 pad 16: +3.3V -> Net-(U3-Pad16)
- U3 pad 4: +3.3V -> Net-(U3-Pad16)
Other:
- board size 121 x 93 mm -> 210 x 103 mm
